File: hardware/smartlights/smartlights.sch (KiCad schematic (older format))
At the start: 23 parts, among them J1 Conn_01x02_MountingPin, J10 Conn_Coaxial_Power, J11 Raspberry_Pi_2_3, J2 Conn_01x04, J3 Conn_01x02_MountingPin, J4 Conn_01x02_MountingPin, J5 Conn_01x02_MountingPin, J6 Conn_01x02_MountingPin, J7 Conn_01x02_MountingPin, J8 Conn_01x02_MountingPin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

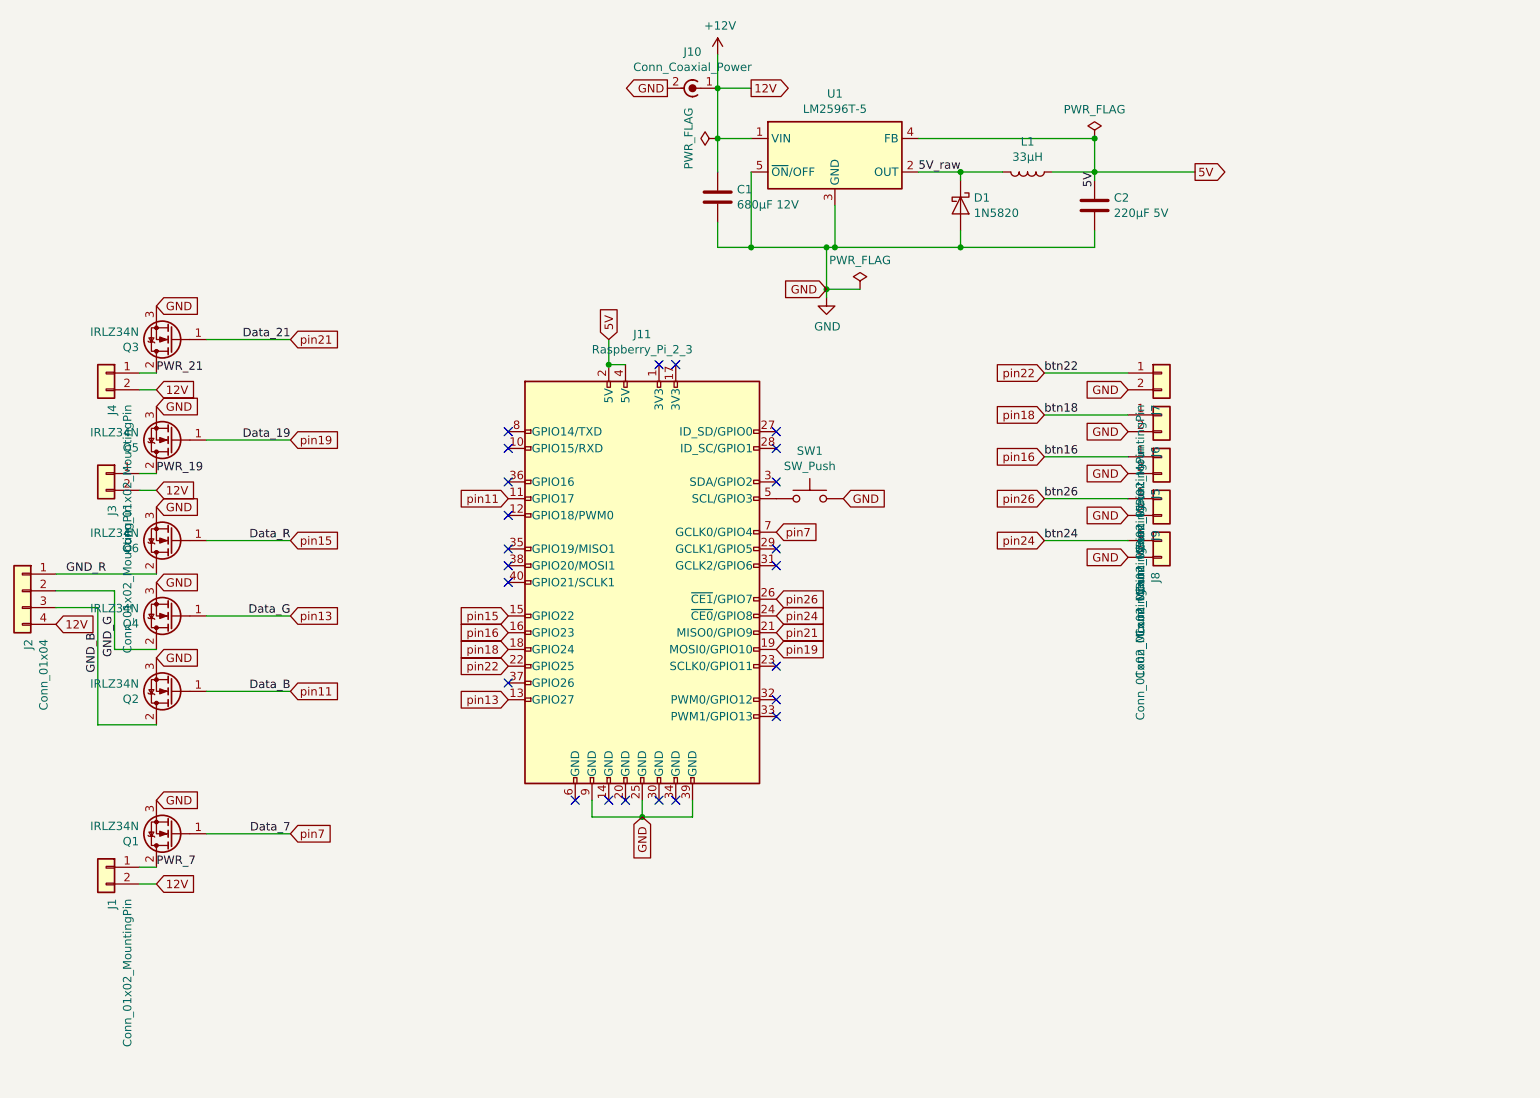
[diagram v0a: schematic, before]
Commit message: SMD Rework
- removed one button to make space
- slightly larger PCB dimensions
- SMD transistor & voltage regulator
- access to individual RGB channels
- second RGB output
- two additional single-color outputs
- power jack moved closer towards edge
- custom footprints for light connectors
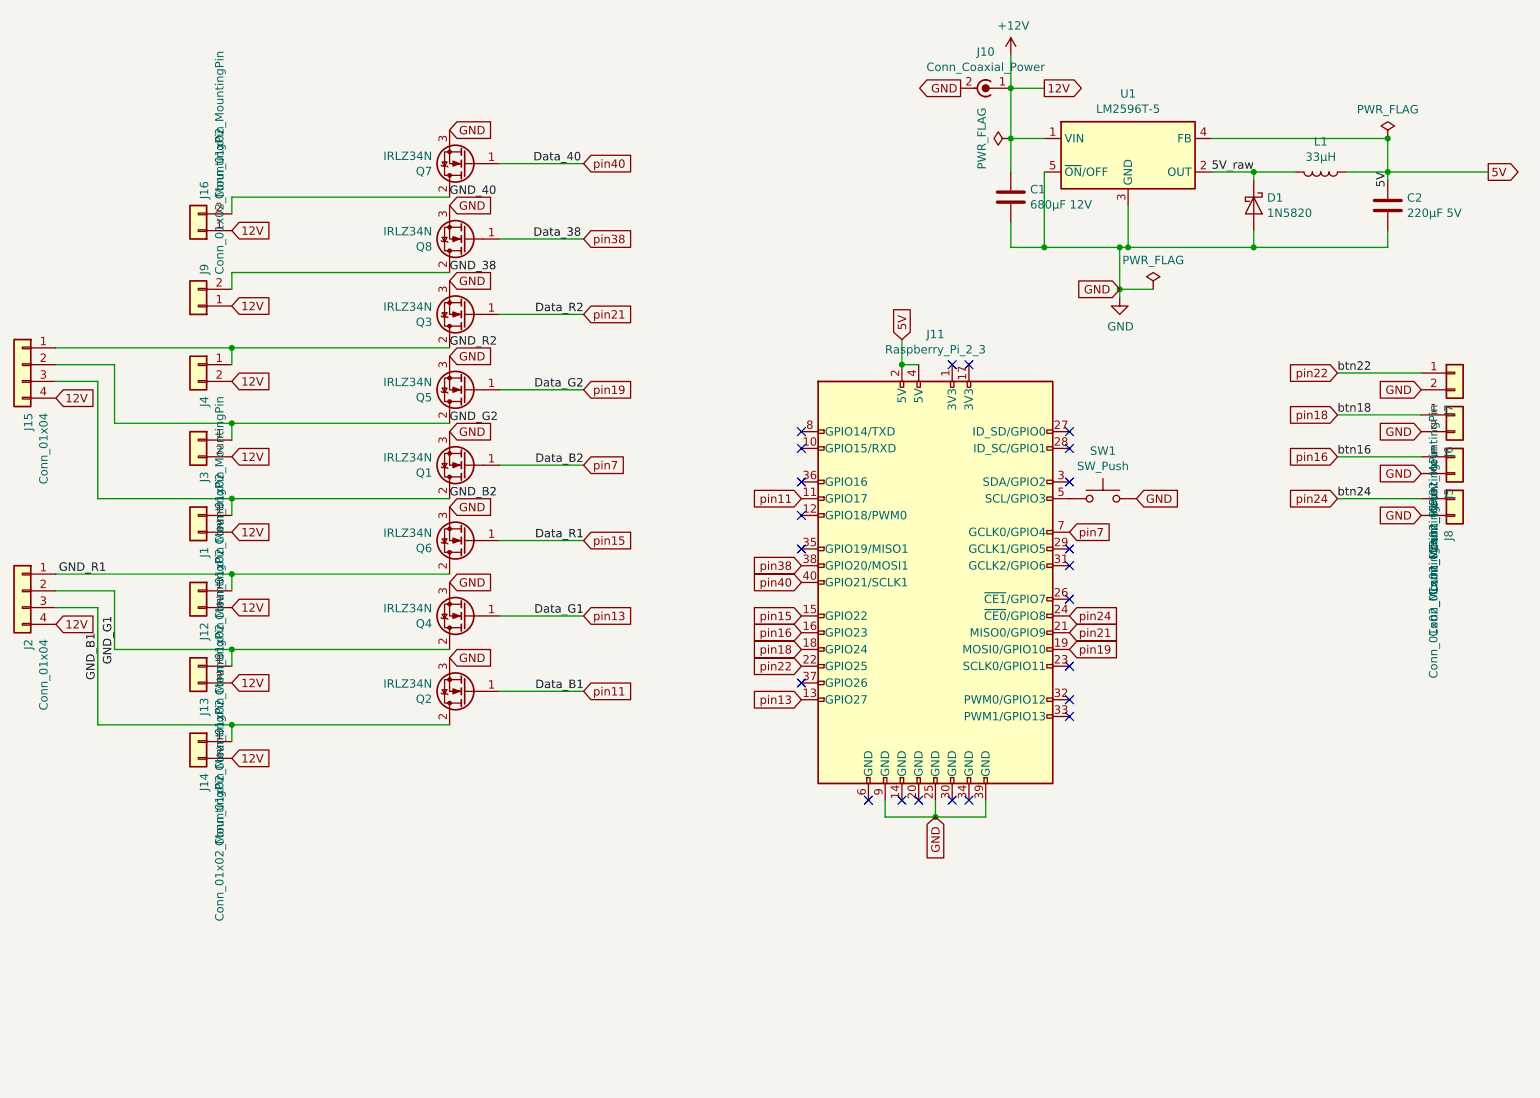
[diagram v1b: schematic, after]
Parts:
- added J12, J13, J14, J16: Conn_01x02_MountingPin, smartlights:PinHeader_1x02_P2.54mm_Vertical_Lock, symbol Connector_Generic:Conn_01x02
- added J15: Conn_01x04, smartlights:PinHeader_1x04_P2.54mm_Vertical_Lock, symbol Connector_Generic:Conn_01x04
- added Q7, Q8: IRLZ34N, smartlights:TO-252AA, symbol Transistor_FET:IRLZ34N
- J1, J3, J4, J5, J6, J7, J8, J9: footprint Connector_PinHeader_2.54mm:PinHeader_1x02_P2.54mm_Vertical -> smartlights:PinHeader_1x02_P2.54mm_Vertical_Lock
- J2: footprint Connector_PinHeader_2.54mm:PinHeader_1x04_P2.54mm_Vertical -> smartlights:PinHeader_1x04_P2.54mm_Vertical_Lock
- Q1, Q2, Q3, Q4, Q5, Q6: footprint Package_TO_SOT_THT:TO-220-3_Vertical -> smartlights:TO-252AA
- U1: footprint Package_TO_SOT_THT:TO-220-5_P3.4x3.7mm_StaggerOdd_Lead3.8mm_Vertical -> Package_TO_SOT_SMD:TO-263-5_TabPin3
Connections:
- net +12V: now also J9.1 (Pin_1), J12.2 (Pin_2), J13.2 (Pin_2), J14.2 (Pin_2), J15.4 (Pin_4), J16.1 (Pin_1)
- net GND: now also Q7.3 (S), Q8.3 (S); no longer J9.2 (Pin_2)
- net pin38: now reaches J11.38 (GPIO20/MOSI1)
- net pin38: now also Q8.1 (G)
- net pin40: now reaches J11.40 (GPIO21/SCLK1)
- net pin40: now also Q7.1 (G)
- net GND_B renamed GND_B1
- net GND_B1: now also J14.1 (Pin_1)
- net GND_G renamed GND_G1
- net GND_G1: now also J13.1 (Pin_1)
- net GND_R renamed GND_R1
- net GND_R1: now also J12.1 (Pin_1)
- net PWR_19 renamed GND_G2
- net GND_G2: now also J15.2 (Pin_2)
- net PWR_21 renamed GND_R2
- net GND_R2: now also J15.1 (Pin_1)
- net PWR_7 renamed GND_B2
- net GND_B2: now also J15.3 (Pin_3)
- net pin26: no longer names the net of J11.26 (~CE1~/GPIO7)
- net pin26: no longer J9.1 (Pin_1)
- new net GND_38: J9.2 (Pin_2), Q8.2 (D)
- new net GND_40: J16.2 (Pin_2), Q7.2 (D)
- no-connect marks 23 -> 22
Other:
- moved on the sheet: C1, C2, D1, J1, J10, J11, J3, J4, J5, J6, J7, J8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
